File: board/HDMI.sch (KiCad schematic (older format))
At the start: 85 parts, among them J2 HDMI, J3 HDMI, J4 HDMI, J5 HDMI, P10 CONN_1, P2 CONN_1, P4 CONN_1, P5 CONN_1, P6 CONN_1, P7 CONN_1, P8 CONN_1, P9 CONN_1, U13 IP4776CZ38, U14 IP4776CZ38, U15 IP4776CZ38, U16 ΜA78L00, U21 IP4776CZ38, U22 ΜA78L00, U30 ΜA78L00

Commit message: Importing footprint names into schematic.
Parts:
- C169, C170, C171, C172, C179, C185, R124, R125, R128, R131, R137, R138, R139, R140, R141, R142, R143, R144, R145, R146, R147, R148, R149, R150, R151, R152, R153, R188, R189, R190, R191, R196, R197, R198, R199, R200, R201, R203, R204, R205: footprint ~ -> SM0402
- C173, C175, C177, C181, C183, C205, C206, C208, C252, R121, R126, R127, R129, R130, R132, R133, R134, R135, R136, R192, R193, R194, R195, R202, R84, R88: footprint ~ -> SM0603
- J2, J3, J4, J5: footprint ~ -> HDMI_TH
- P10, P2, P4, P5, P6, P7, P8, P9: footprint (none) -> 1Pin_N
- U13, U14, U15, U21: footprint (none) -> SSOP38_ip4776
- U16, U22, U30: footprint (none) -> μA78L00

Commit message: Adding test points to CEC and HPD lines.
https://github.com/timvideos/HDMI2USB-numato-opsis-hardware/issues/17
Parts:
- added P19, P20, P21, P22, P23, P24, P25, P26: CONN_1, 1Pin_N, symbol CONN_1
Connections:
- net TMDS-RX1-CEC: now also P19.1
- net TMDS-RX1-HOT: now also P24.1
- net TMDS-RX2-CEC: now also P25.1
- net TMDS-RX2-HOT: now also P26.1
- net TMDS-TX1-CEC: now also P20.1
- net TMDS-TX1-HOT: now also P21.1
- net TMDS-TX2-CEC: now also P22.1
- net TMDS-TX2-HOT: now also P23.1
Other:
- moved on the sheet: P10, P2, P4, P5, P6, P7, P8, P9, R126, R127, R129, R130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

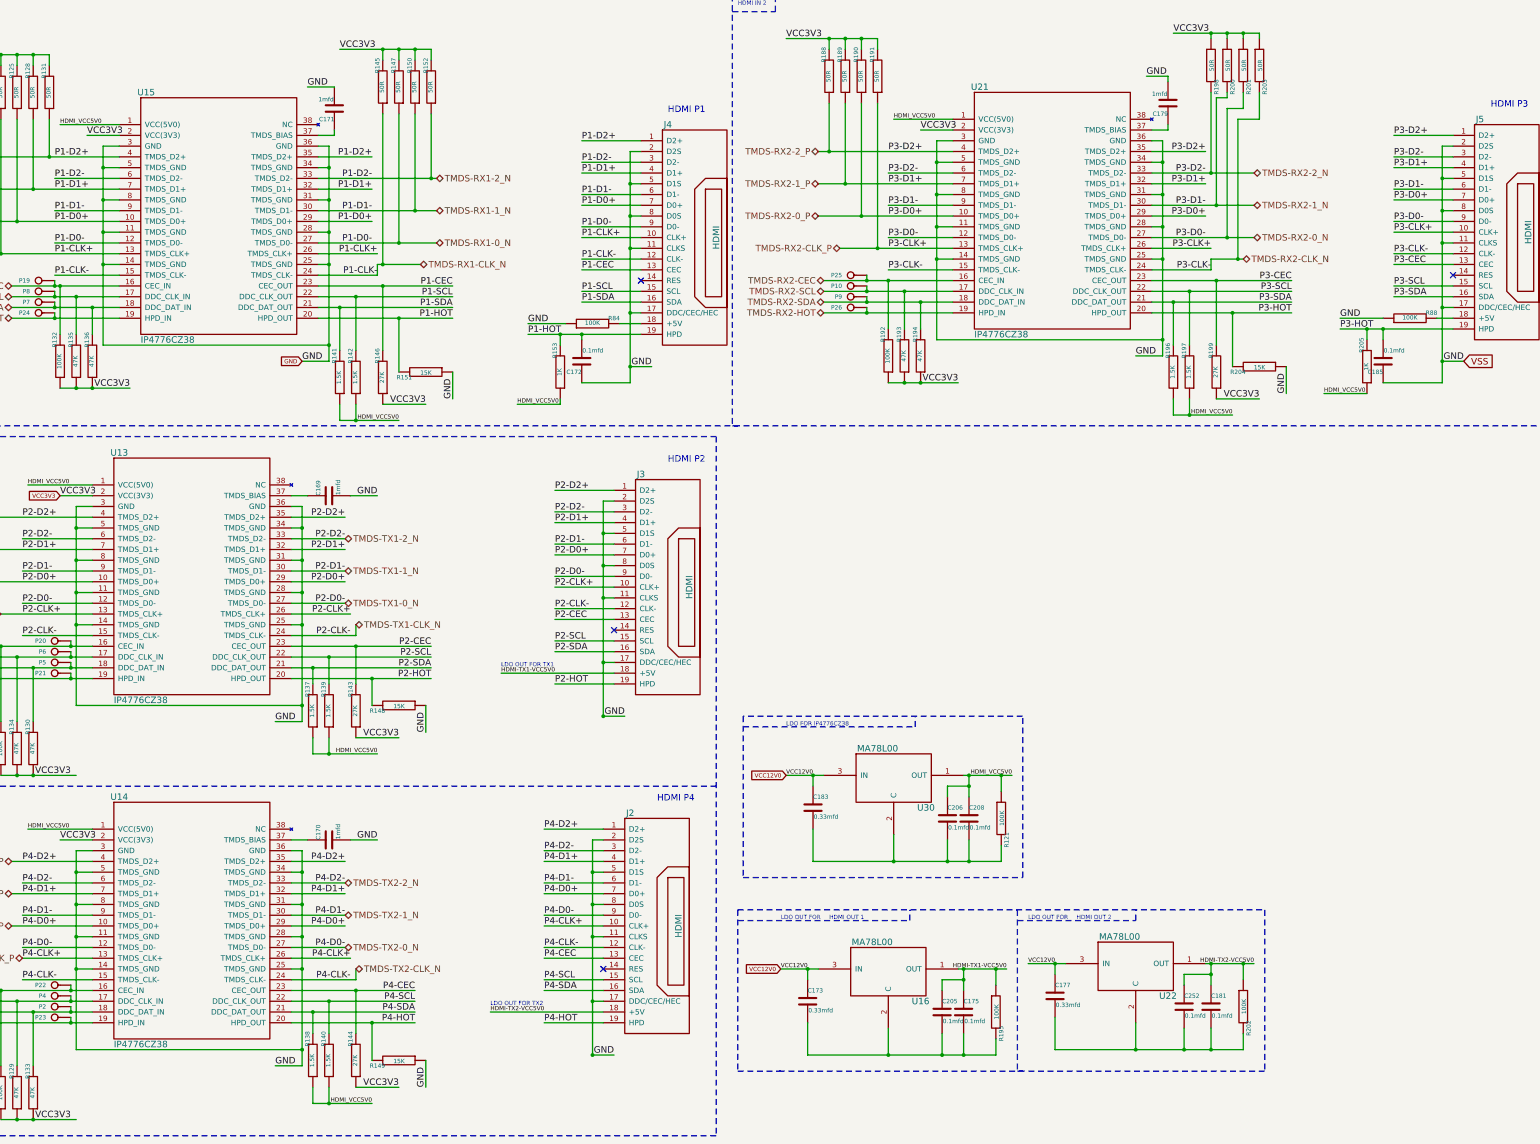
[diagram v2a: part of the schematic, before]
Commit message: Fixing up GND references in the HDMI sheet.
https://github.com/timvideos/HDMI2USB-numato-opsis-hardware/issues/19
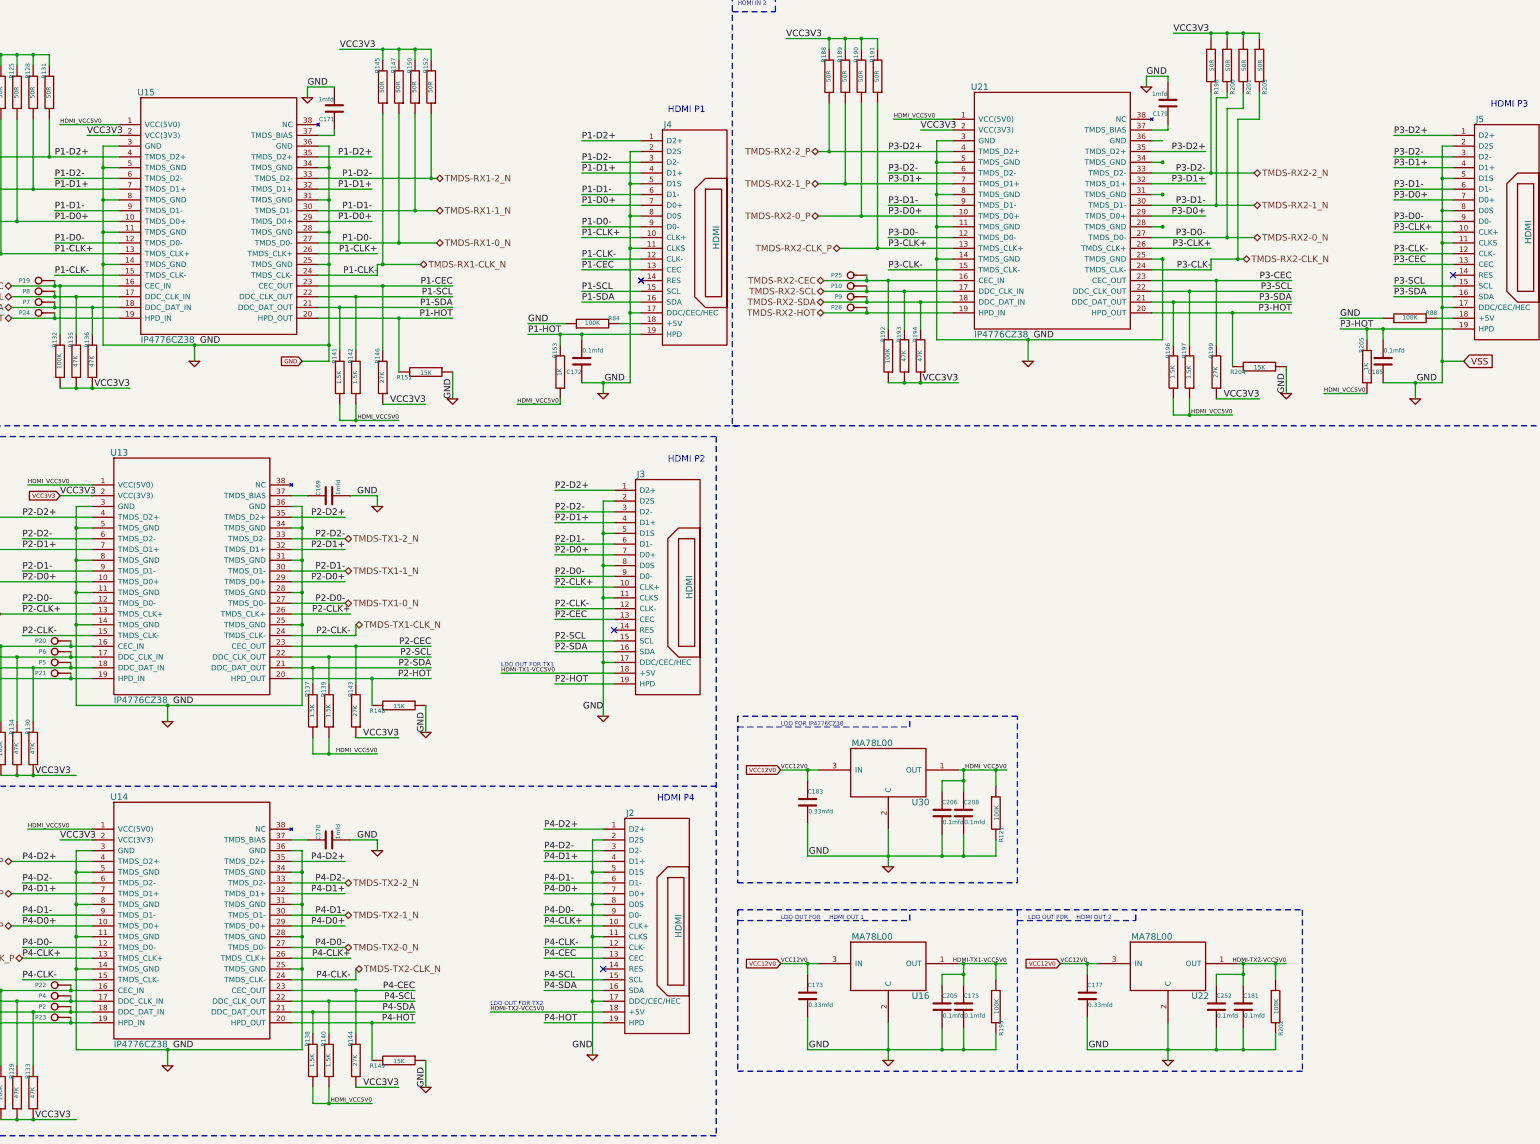
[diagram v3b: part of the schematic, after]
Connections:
- net GND: now also C173.2, C175.2, C177.2, C181.2, C183.2, C205.2, C206.2, C208.2, C252.2, R121.2, R195.2, R202.2, U16.2 (C), U22.2 (C), U30.2 (C); no longer U21.28 (TMDS_GND), U21.31 (TMDS_GND), U21.34 (TMDS_GND), U21.36 (GND)
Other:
- moved on the sheet: C173, C175, C177, C181, C183, C205, C206, C208, C252, R121, R195, R202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

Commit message: Fixing DRC errors.
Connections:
- net GND: now also U21.28 (TMDS_GND), U21.31 (TMDS_GND), U21.34 (TMDS_GND), U21.36 (GND)

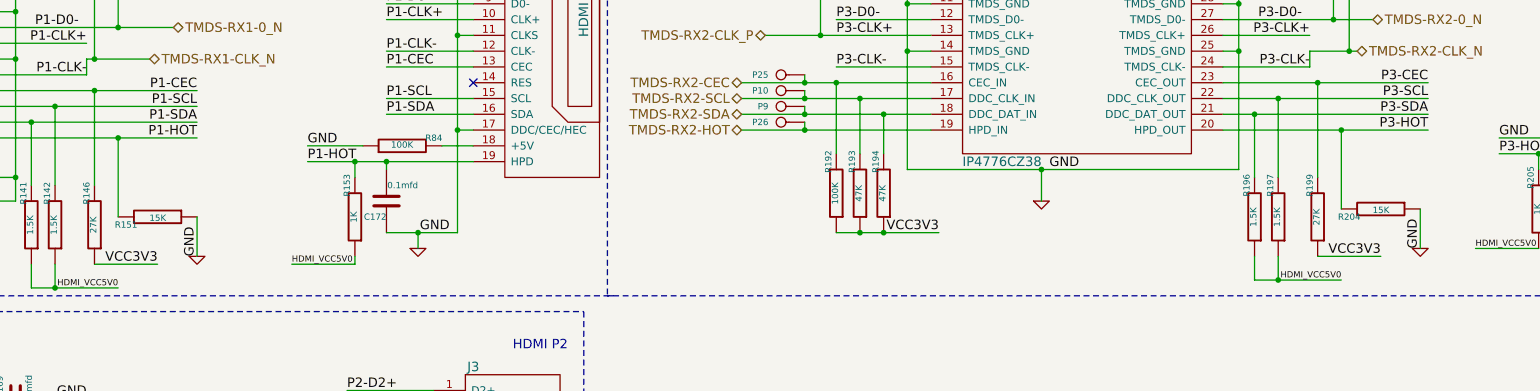
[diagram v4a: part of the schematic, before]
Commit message: Removing R151,R204
https://github.com/timvideos/HDMI2USB-numato-opsis-hardware/issues/16
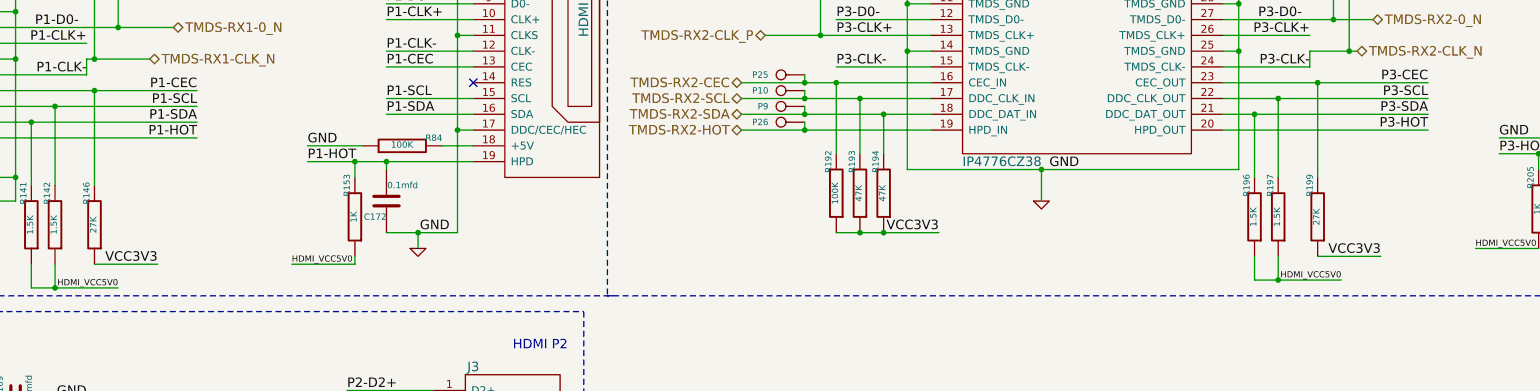
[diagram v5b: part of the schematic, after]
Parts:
- removed R151, R204: 15K, SM0402, symbol R
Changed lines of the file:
@@
 $EndComp
-$Comp
-L R R151
-U 1 1 520C6646
-P 5400 4000
-F 0 "R151" V 5450 3800 40  0000 C CNN
-F 1 "15K" V 5407 4001 40  0000 C CNN
-F 2 "SM0402" V 5330 4000 30  0001 C CNN
-F 3 "~" H 5400 4000 30  0000 C CNN
-F 4 "Yes" H 5400 4000 30  0001 C CNN "Populate"
-	1    5400 4000
-	0    1    1    0
-$EndComp
-Text Label 5650 4250 1    60   ~ 0
-GND
 $Comp
 L R R146
@@
 	-1   0    0    1
 $EndComp
-$Comp
-L R R204
-U 1 1 520C87E9
-P 13150 3950
-F 0 "R204" V 13200 3750 40  0000 C CNN
-F 1 "15K" V 13157 3951 40  0000 C CNN
-F 2 "SM0402" V 13080 3950 30  0001 C CNN
-F 3 "~" H 13150 3950 30  0000 C CNN
-F 4 "Yes" H 13150 3950 30  0001 C CNN "Populate"
-	1    13150 3950
-	0    1    1    0
-$EndComp
-Text Label 13400 4200 1    60   ~ 0
-GND
 $Comp
 L R R199
@@
 Wire Wire Line
 	4900 7100 4900 6850
-Connection ~ 12900 3450
-Wire Wire Line
-	12900 3950 12900 3450
 Connection ~ 1750 10950
 Wire Wire Line
@@
 	12750 3750 12750 3150
 Wire Wire Line
-	13400 3950 13400 4200
-Wire Wire Line
 	12750 4250 13150 4250
 Wire Wire Line
@@
 Wire Wire Line
 	5000 3800 5000 3200
-Connection ~ 5150 3500
 Wire Wire Line
 	12700 3050 12700 2950
@@
 Wire Wire Line
 	4400 3500 5650 3500
-Wire Wire Line
-	5650 4000 5650 4250
-Wire Wire Line
-	5150 3500 5150 4000
 Wire Wire Line
 	5000 4300 5400 4300
@@
 Connection ~ 14600 4100
 $Comp
-L GND #PWR049
-U 1 1 55DEA9FC
-P 5650 4250
-F 0 "#PWR049" H 5650 4250 30  0001 C CNN
-F 1 "GND" H 5650 4180 30  0001 C CNN
-F 2 "" H 5650 4250 60  0000 C CNN
-F 3 "" H 5650 4250 60  0000 C CNN
-	1    5650 4250
-	1    0    0    -1
-$EndComp
-$Comp
 L GND #PWR050
 U 1 1 55DEAA02
@@
 	12250 1850 12250 3700
 $Comp
-L GND #PWR052
-U 1 1 55DEB156
-P 13400 4200
-F 0 "#PWR052" H 13400 4200 30  0001 C CNN
-F 1 "GND" H 13400 4130 30  0001 C CNN
-F 2 "" H 13400 4200 60  0000 C CNN
-F 3 "" H 13400 4200 60  0000 C CNN
-	1    13400 4200
-	1    0    0    -1
-$EndComp
-$Comp
 L GND #PWR053

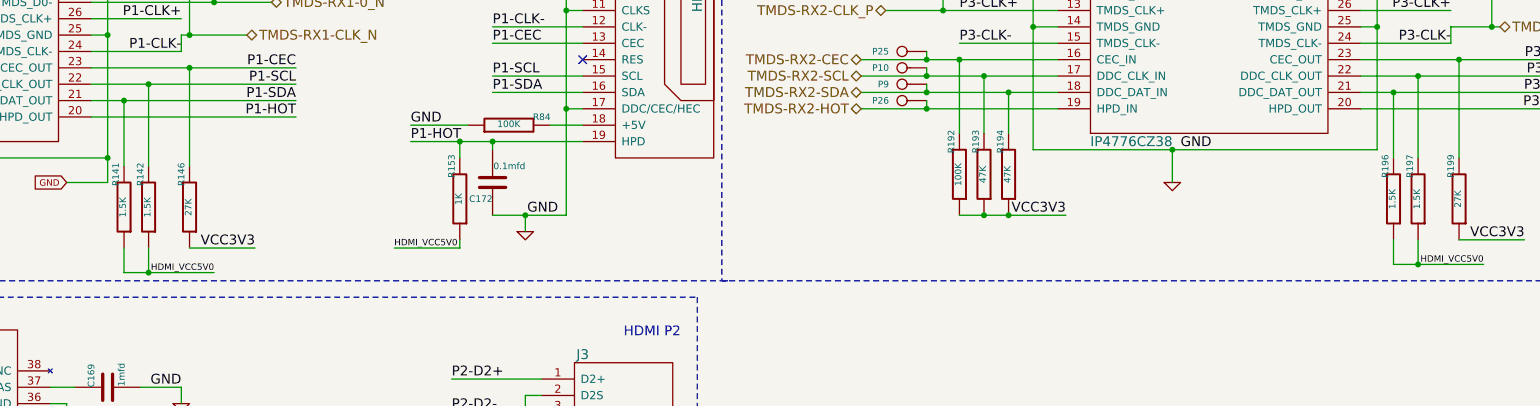
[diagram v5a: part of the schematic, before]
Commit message: Fixing values of R141,R142,R197,R196
https://github.com/timvideos/HDMI2USB-numato-opsis-hardware/issues/16
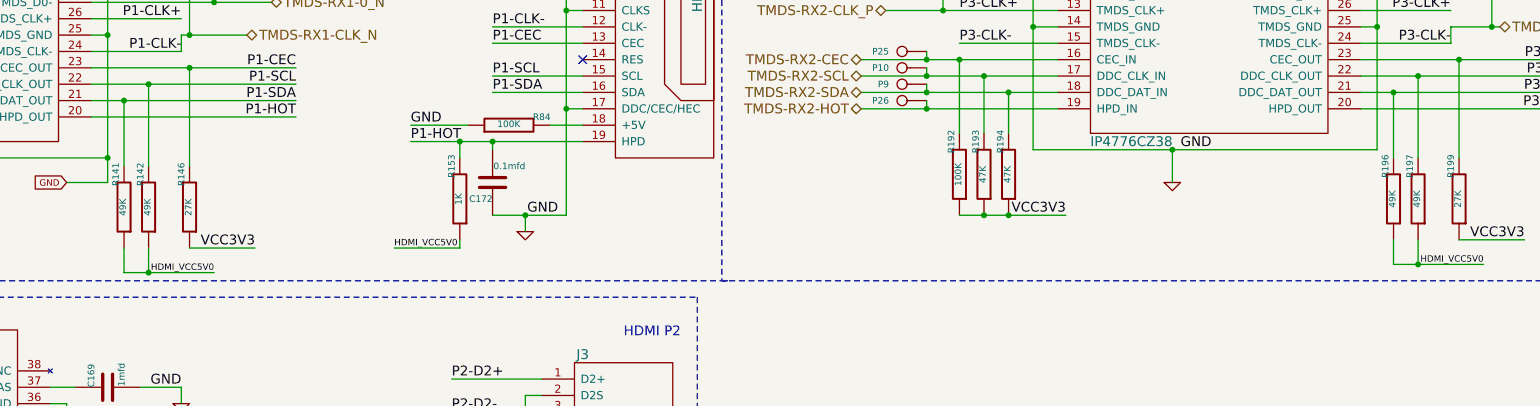
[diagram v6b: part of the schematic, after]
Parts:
- R141, R142, R196, R197: value 1.5K -> 49K
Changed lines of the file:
@@
 P 4600 4050
 F 0 "R141" V 4650 3850 40  0000 C CNN
-F 1 "1.5K" V 4607 4051 40  0000 C CNN
+F 1 "49K" V 4607 4051 40  0000 C CNN
 F 2 "SM0402" V 4530 4050 30  0001 C CNN
 F 3 "~" H 4600 4050 30  0000 C CNN
@@
 P 4750 4050
 F 0 "R142" V 4800 3850 40  0000 C CNN
-F 1 "1.5K" V 4757 4051 40  0000 C CNN
+F 1 "49K" V 4757 4051 40  0000 C CNN
 F 2 "SM0402" V 4680 4050 30  0001 C CNN
 F 3 "~" H 4750 4050 30  0000 C CNN
@@
 P 12350 4000
 F 0 "R196" V 12400 3800 40  0000 C CNN
-F 1 "1.5K" V 12357 4001 40  0000 C CNN
+F 1 "49K" V 12357 4001 40  0000 C CNN
 F 2 "SM0402" V 12280 4000 30  0001 C CNN
 F 3 "~" H 12350 4000 30  0000 C CNN
@@
 P 12500 4000
 F 0 "R197" V 12550 3800 40  0000 C CNN
-F 1 "1.5K" V 12507 4001 40  0000 C CNN
+F 1 "49K" V 12507 4001 40  0000 C CNN
 F 2 "SM0402" V 12430 4000 30  0001 C CNN
 F 3 "~" H 12500 4000 30  0000 C CNN
